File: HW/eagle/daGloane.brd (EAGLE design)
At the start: 100 x 80 mm, 83 parts, among them IC1 MCP1252-33X50, U1 STM32F10XTXU6, X2 SPARKFUN-CONNECTORS_USB-MICROB

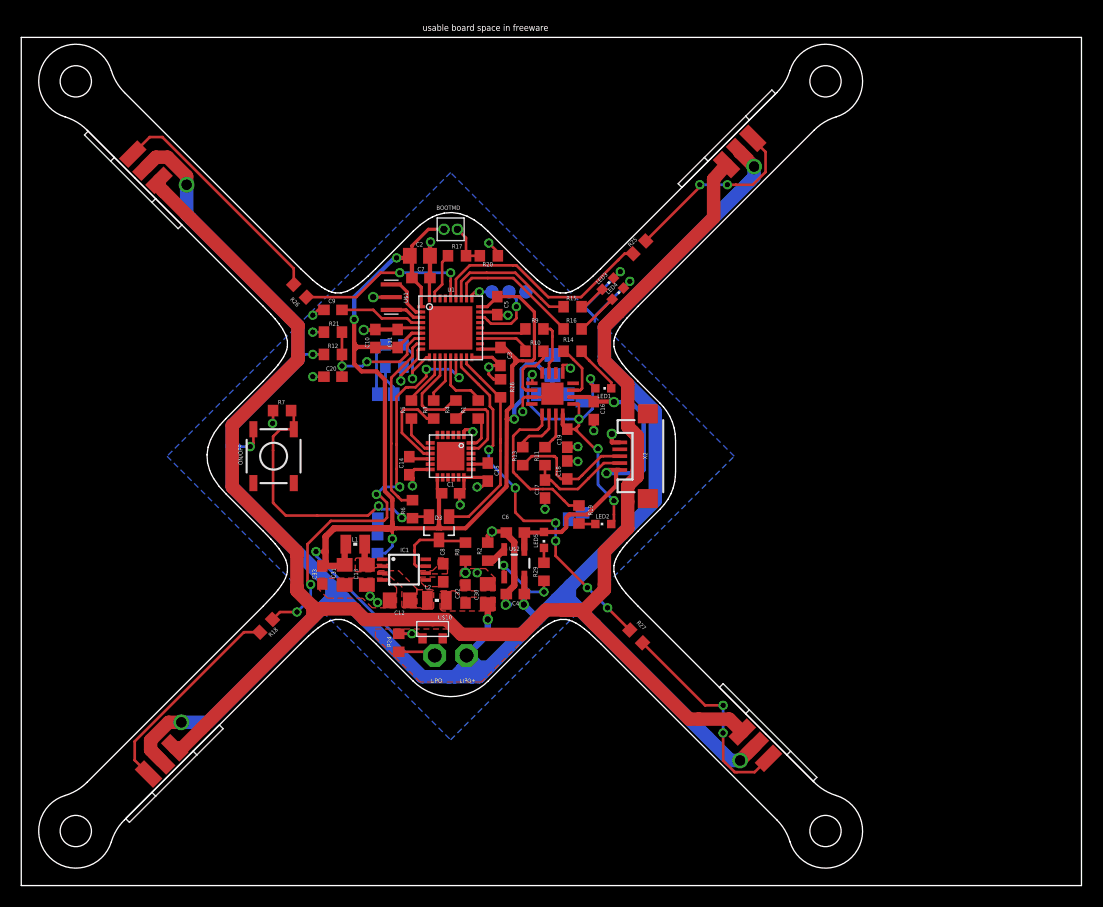
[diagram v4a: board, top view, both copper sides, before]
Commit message: orientation of BLDC controllers changed
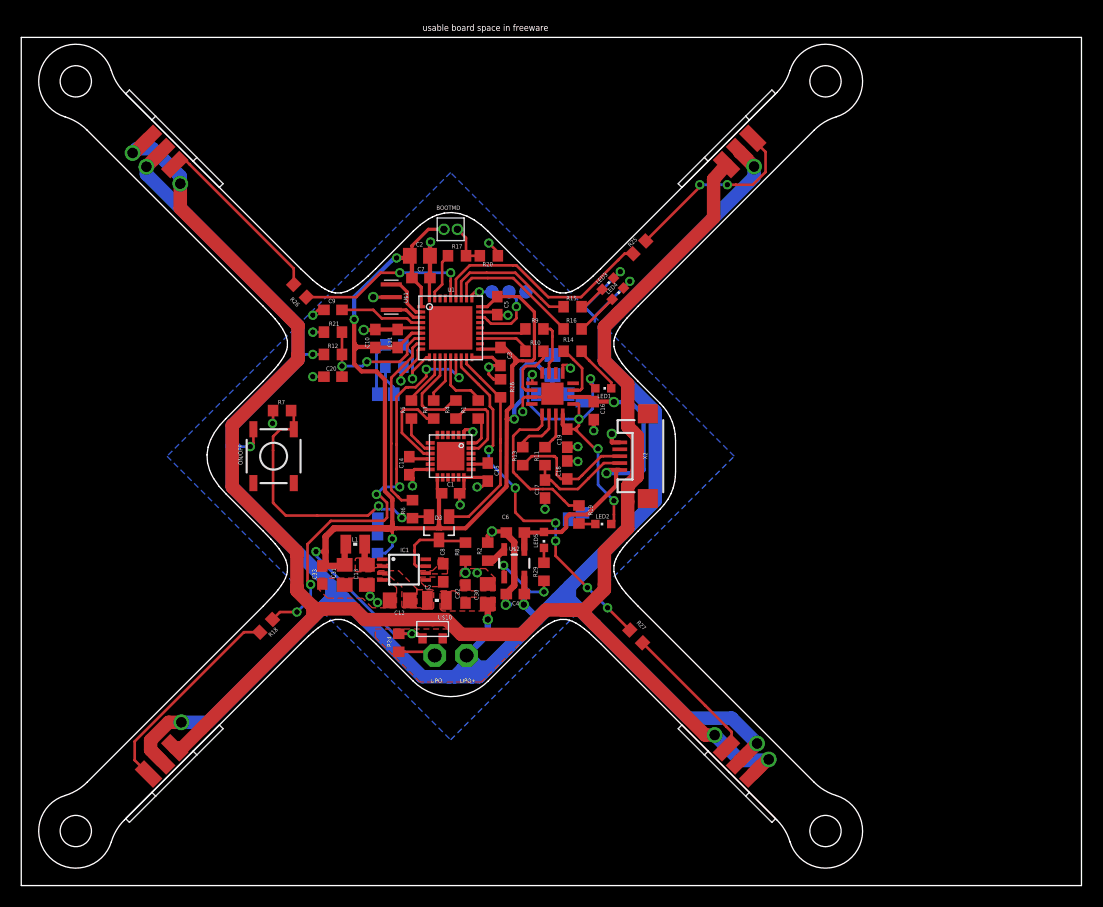
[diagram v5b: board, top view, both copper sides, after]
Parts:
- turned U$7 to 225 degrees
- turned U$9 to 45 degrees
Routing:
- net MOT_GND: track 170.9 -> 184.7 mm, vias 0 -> 4
- net N$39: track 20.5 -> 13.6 mm, vias 2 -> 0
- net N$41: track 22.5 -> 17.3 mm
- net LIPO: track 219.4 -> 218.5 mm

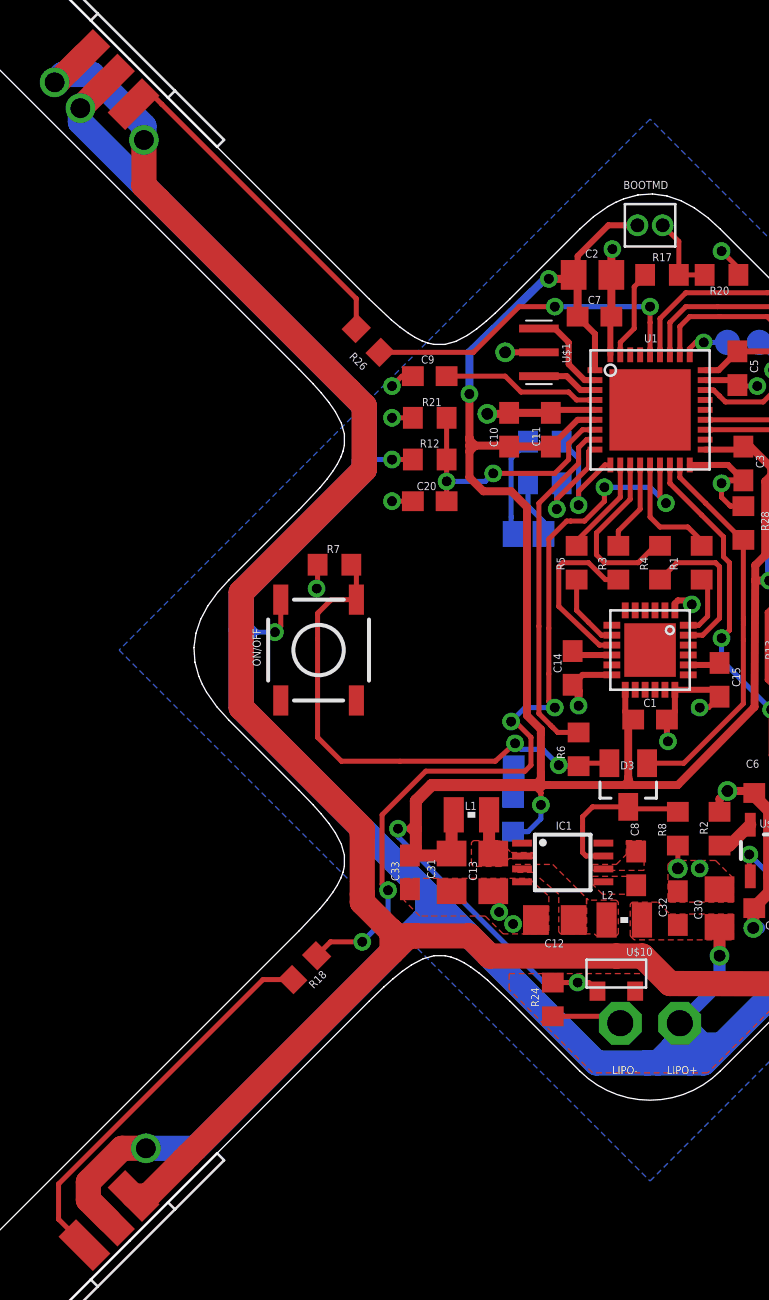
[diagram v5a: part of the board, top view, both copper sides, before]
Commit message: GND shape outline changed
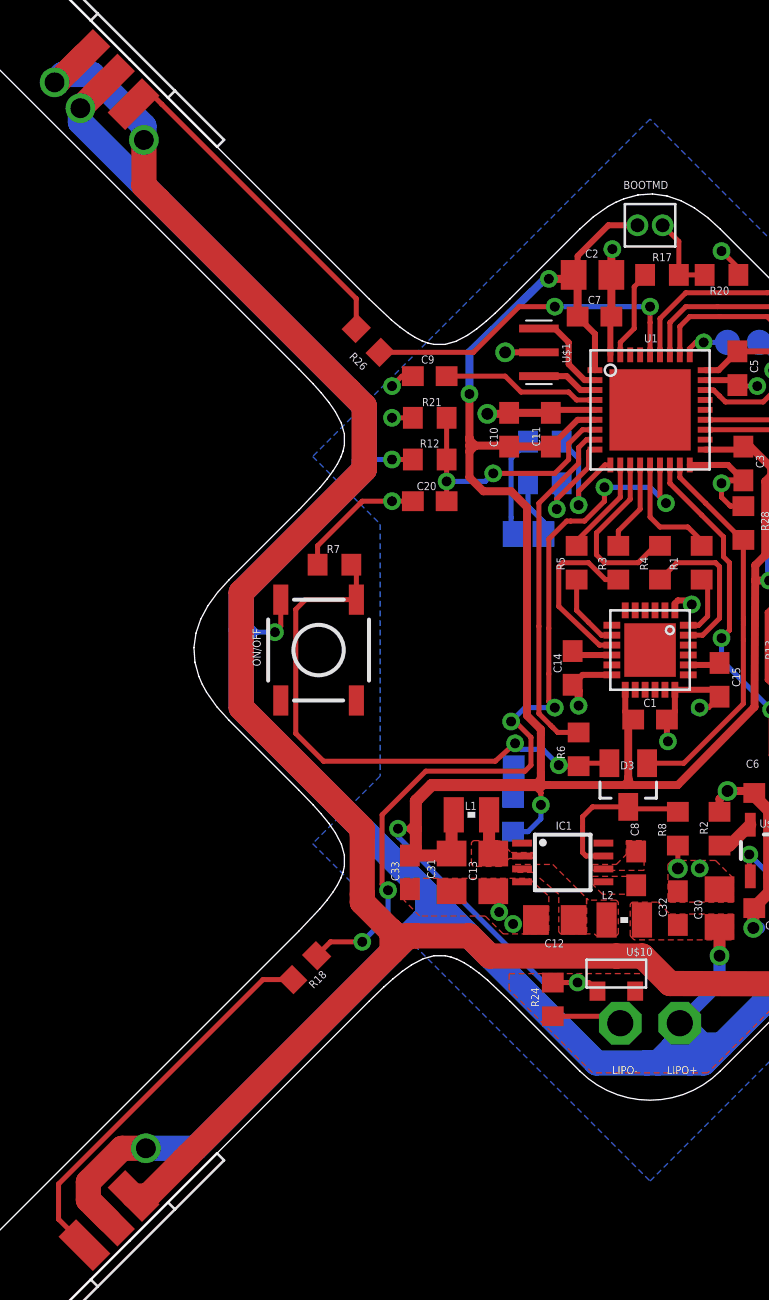
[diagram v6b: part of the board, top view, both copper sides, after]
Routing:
- net GND: track 79.7 -> 83.8 mm, vias 29 -> 28
- net N$23: track 26.8 -> 28.6 mm
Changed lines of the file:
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@@
 <hole x="5.144659375" y="75.8553375" drill="2.95"/>
 <polygon width="0.254" layer="42">
-<vertex x="26.5" y="33.9"/>
-<vertex x="26.5" y="46.9"/>
+<vertex x="25.8" y="33.9"/>
+<vertex x="25.8" y="46.9"/>
 <vertex x="32" y="46.9"/>
 <vertex x="32" y="45.1"/>
@@
 <via x="42.6" y="42.8" extent="1-16" drill="0.5"/>
 <polygon width="0.4" layer="16" isolate="0.254" thermals="no">
-<vertex x="13.75" y="40.5"/>
+<vertex x="23.5" y="50.25"/>
+<vertex x="26.9" y="46.85"/>
+<vertex x="26.9" y="34.15"/>
+<vertex x="23.5" y="30.75"/>
 <vertex x="40.5" y="13.75"/>
 <vertex x="67.25" y="40.5"/>
@@
 <wire x1="54.1" y1="53.7" x2="54.1" y2="53.6" width="0.254" layer="16"/>
 <wire x1="54.1" y1="53.6" x2="54.1" y2="53.2" width="0.254" layer="16"/>
-<wire x1="23.75" y1="44.8" x2="23.75" y2="43.65" width="0.254" layer="1"/>
-<wire x1="23.75" y1="43.65" x2="23.7" y2="43.6" width="0.254" layer="1"/>
-<via x="23.7" y="43.6" extent="1-16" drill="0.5"/>
-<wire x1="23.7" y1="43.6" x2="23.4" y2="43.6" width="0.254" layer="16"/>
 <wire x1="35.6" y1="22.05" x2="38.65" y2="22.05" width="0.254" layer="1"/>
 <wire x1="38.65" y1="22.05" x2="39" y2="21.7" width="0.254" layer="1"/>
@@
 <wire x1="57.4" y1="57" x2="54.1" y2="53.7" width="0.254" layer="16"/>
 <wire x1="54.1" y1="53.6" x2="53.1" y2="54.6" width="0.254" layer="16"/>
+<wire x1="23.75" y1="44.8" x2="23.75" y2="45.75" width="0.254" layer="1"/>
+<wire x1="23.75" y1="45.75" x2="25.9" y2="47.9" width="0.254" layer="1"/>
+<wire x1="25.9" y1="47.9" x2="26" y2="48" width="0.254" layer="1"/>
+<wire x1="26" y1="48" x2="27.5" y2="48" width="0.254" layer="1"/>
 </signal>
 <signal name="LED1">
@@
 <contactref element="R6" pad="1"/>
 <contactref element="D3" pad="2"/>
-<wire x1="25.45" y1="44.8" x2="25.705" y2="44.545" width="0.254" layer="1"/>
-<wire x1="23.8" y1="42.4" x2="24.4" y2="43" width="0.254" layer="1"/>
 <via x="35.9" y="34.7" extent="1-16" drill="0.5"/>
 <wire x1="35.9" y1="34.7" x2="35.1" y2="35.5" width="0.254" layer="16"/>
@@
 <via x="33.7" y="35.8" extent="1-16" drill="0.5"/>
 <wire x1="33.7" y1="35.8" x2="32.7" y2="34.9" width="0.254" layer="1"/>
-<wire x1="32.7" y1="34.9" x2="27.9" y2="34.9" width="0.254" layer="1"/>
-<wire x1="27.9" y1="34.9" x2="24.95" y2="34.9" width="0.254" layer="1"/>
-<wire x1="24.95" y1="34.9" x2="23.75" y2="36.1" width="0.254" layer="1"/>
-<wire x1="23.75" y1="36.1" x2="23.75" y2="41.05" width="0.254" layer="1"/>
+<wire x1="32.7" y1="34.9" x2="24.05" y2="34.9" width="0.254" layer="1"/>
+<wire x1="24.05" y1="34.9" x2="22.65" y2="36.3" width="0.254" layer="1"/>
+<wire x1="22.65" y1="36.3" x2="22.65" y2="42.55" width="0.254" layer="1"/>
 <wire x1="35.9" y1="34.7" x2="35.95" y2="34.65" width="0.254" layer="1"/>
 <wire x1="35.95" y1="34.65" x2="36.9" y2="34.65" width="0.254" layer="1"/>
-<wire x1="23.75" y1="41.05" x2="23.75" y2="42.35" width="0.254" layer="1"/>
-<wire x1="23.75" y1="42.35" x2="23.8" y2="42.4" width="0.254" layer="1"/>
 <wire x1="36.9" y1="34.65" x2="37.15" y2="34.8" width="0.254" layer="1"/>
 <wire x1="37.15" y1="34.8" x2="38.45" y2="34.8" width="0.254" layer="1"/>
-<wire x1="25.705" y1="43.04" x2="24.44" y2="43.04" width="0.254" layer="1"/>
-<wire x1="24.44" y1="43.04" x2="24.4" y2="43" width="0.254" layer="1"/>
+<wire x1="25.705" y1="43.04" x2="23.14" y2="43.04" width="0.254" layer="1"/>
 <wire x1="25.705" y1="43.04" x2="25.705" y2="44.545" width="0.254" layer="1"/>
 <wire x1="25.705" y1="44.545" x2="25.45" y2="44.8" width="0.254" layer="1"/>
+<wire x1="22.65" y1="42.55" x2="23.14" y2="43.04" width="0.254" layer="1"/>
 </signal>
 <signal name="N$2">
